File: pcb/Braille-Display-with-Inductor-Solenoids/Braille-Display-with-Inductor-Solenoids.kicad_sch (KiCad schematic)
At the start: 15 parts, among them J1 Screw_Terminal_01x02, J2 Screw_Terminal_01x02, J3 Screw_Terminal_01x02, SW1 SW_Push, SW2 SW_Push, U1 RP2040-Zero

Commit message: Remove symbol and footprint libraries
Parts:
- removed U1: RP2040-Zero, 00-project-footprint-lib:RP2040 Zero, symbol 00-project-symbol-lib:RP2040-Zero
- added U1: RP2040-Zero, 00-project-footprints:RP2040 Zero, symbol 00-project-symbols:RP2040-Zero
- SW1, SW2: footprint 00-project-footprint-lib:PushButtonSMD_2.93x3.9 -> 00-project-footprints:PushButtonSMD_2.93x3.9
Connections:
- net +3V3: now also U1.3 (3V3)
- net +5V: now also U1.1 (5V)
- net GND: now also U1.2 (GND)
- net SHIFT_G: now also U1.15 (GP5)
- net SHIFT_RCLK: now also U1.14 (GP4)
- net SHIFT_SER_IN: now also U1.12 (GP2)
- net SHIFT_SRCK: now also U1.13 (GP3)
- net SW_1: now also U1.5 (GP28)
- net SW_2: now also U1.6 (GP27)
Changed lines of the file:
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@@
 			)
 		)
-		(property "Footprint" "00-project-footprint-lib:PushButtonSMD_2.93x3.9"
+		(property "Footprint" "00-project-footprints:PushButtonSMD_2.93x3.9"
 			(at 67.31 158.75 0)
 			(effects
@@
 				(path "/3829a125-89bd-48f9-bfbe-92d753eb8f7f"
 					(reference "SW1")
-					(unit 1)
-				)
-			)
-		)
-	)
-	(symbol
-		(lib_id "00-project-symbol-lib:RP2040-Zero")
-		(at 64.77 48.26 0)
-		(unit 1)
-		(exclude_from_sim no)
-		(in_bom yes)
-		(on_board yes)
-		(dnp no)
-		(fields_autoplaced yes)
-		(property "Reference" "U1"
-			(at 64.77 35.56 0)
-			(effects
-				(font
-					(size 1.27 1.27)
-				)
-			)
-		)
-		(property "Value" "RP2040-Zero"
-			(at 64.77 38.1 0)
-			(effects
-				(font
-					(size 1.27 1.27)
-				)
-			)
-		)
-		(property "Footprint" "00-project-footprint-lib:RP2040 Zero"
-			(at 59.69 48.26 0)
-			(effects
-				(font
-					(size 1.27 1.27)
-				)
-				(hide yes)
-			)
-		)
-		(property "Datasheet" ""
-			(at 59.69 48.26 0)
-			(effects
-				(font
-					(size 1.27 1.27)
-				)
-				(hide yes)
-			)
-		)
-		(property "Description" ""
-			(at 64.77 48.26 0)
-			(effects
-				(font
-					(size 1.27 1.27)
-				)
-				(hide yes)
-			)
-		)
-		(pin "2"
-		)
-		(pin "21"
-		)
-		(pin "9"
-		)
-		(pin "17"
-		)
-		(pin "8"
-		)
-		(pin "19"
-		)
-		(pin "5"
-		)
-		(pin "18"
-		)
-		(pin "6"
-		)
-		(pin "20"
-		)
-		(pin "7"
-		)
-		(pin "4"
-		)
-		(pin "3"
-		)
-		(pin "23"
-		)
-		(pin "11"
-		)
-		(pin "14"
-		)
-		(pin "15"
-		)
-		(pin "22"
-		)
-		(pin "13"
-		)
-		(pin "12"
-		)
-		(pin "1"
-		)
-		(pin "10"
-		)
-		(pin "16"
-		)
-		(instances
-			(project ""
-				(path "/3829a125-89bd-48f9-bfbe-92d753eb8f7f"
-					(reference "U1")
 					(unit 1)
 				)
@@
 	)
 	(symbol
+		(lib_id "00-project-symbols:RP2040-Zero")
+		(at 64.77 48.26 0)
+		(unit 1)
+		(exclude_from_sim no)
+		(in_bom yes)
+		(on_board yes)
+		(dnp no)
+		(fields_autoplaced yes)
+		(property "Reference" "U1"
+			(at 64.77 35.56 0)
+			(effects
+				(font
+					(size 1.27 1.27)
+				)
+			)
+		)
+		(property "Value" "RP2040-Zero"
+			(at 64.77 38.1 0)
+			(effects
+				(font
+					(size 1.27 1.27)
+				)
+			)
+		)
+		(property "Footprint" "00-project-footprints:RP2040 Zero"
+			(at 59.69 48.26 0)
+			(effects
+				(font
+					(size 1.27 1.27)
+				)
+				(hide yes)
+			)
+		)
+		(property "Datasheet" ""
+			(at 59.69 48.26 0)
+			(effects
+				(font
+					(size 1.27 1.27)
+				)
+				(hide yes)
+			)
+		)
+		(property "Description" ""
+			(at 64.77 48.26 0)
+			(effects
+				(font
+					(size 1.27 1.27)
+				)
+				(hide yes)
+			)
+		)
+		(pin "14"
+		)
+		(pin "13"
+		)
+		(pin "11"
+		)
+		(pin "12"
+		)
+		(pin "15"
+		)
+		(pin "10"
+		)
+		(pin "8"
+		)
+		(pin "20"
+		)
+		(pin "3"
+		)
+		(pin "21"
+		)
+		(pin "5"
+		)
+		(pin "7"
+		)
+		(pin "16"
+		)
+		(pin "23"
+		)
+		(pin "17"
+		)
+		(pin "19"
+		)
+		(pin "22"
+		)
+		(pin "18"
+		)
+		(pin "2"
+		)
+		(pin "6"
+		)
+		(pin "4"
+		)
+		(pin "9"
+		)
+		(pin "1"
+		)
+		(instances
+			(project ""
+				(path "/3829a125-89bd-48f9-bfbe-92d753eb8f7f"
+					(reference "U1")
+					(unit 1)
+				)
+			)
+		)
+	)
+	(symbol
 		(lib_id "power:+3V3")
 		(at 44.45 48.26 90)
@@
 			)
 		)
-		(property "Footprint" "00-project-footprint-lib:PushButtonSMD_2.93x3.9"
+		(property "Footprint" "00-project-footprints:PushButtonSMD_2.93x3.9"
 			(at 85.09 158.75 0)
 			(effects

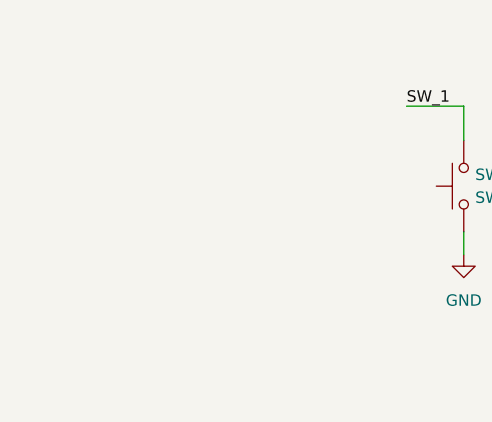
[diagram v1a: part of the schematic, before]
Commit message: Add both inductors on same PCB, switch to new drivers
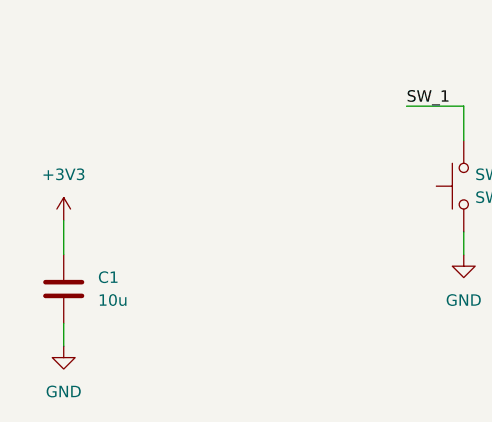
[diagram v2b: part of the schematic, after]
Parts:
- added C1: 10u, Capacitor_SMD:C_1206_3216Metric_Pad1.33x1.80mm_HandSolder, symbol Device:C
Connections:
- net +3V3: now also C1.1
- net GND: now also C1.2
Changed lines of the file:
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@@
+	(wire
+		(pts
+			(xy 27.94 162.56) (xy 27.94 166.37)
+		)
+		(stroke
+			(width 0)
+			(type default)
+		)
+	)
 	(wire
 		(pts
@@
 		(pts
 			(xy 90.17 149.86) (xy 90.17 153.67)
+		)
+		(stroke
+			(width 0)
+			(type default)
+		)
+	)
+	(wire
+		(pts
+			(xy 27.94 173.99) (xy 27.94 176.53)
 		)
 		(stroke
@@
 	)
 	(symbol
+		(lib_id "Device:C")
+		(at 27.94 170.18 0)
+		(unit 1)
+		(exclude_from_sim no)
+		(in_bom yes)
+		(on_board yes)
+		(dnp no)
+		(fields_autoplaced yes)
+		(property "Reference" "C1"
+			(at 31.75 168.9099 0)
+			(effects
+				(font
+					(size 1.27 1.27)
+				)
+				(justify left)
+			)
+		)
+		(property "Value" "10u"
+			(at 31.75 171.4499 0)
+			(effects
+				(font
+					(size 1.27 1.27)
+				)
+				(justify left)
+			)
+		)
+		(property "Footprint" "Capacitor_SMD:C_1206_3216Metric_Pad1.33x1.80mm_HandSolder"
+			(at 28.9052 173.99 0)
+			(effects
+				(font
+					(size 1.27 1.27)
+				)
+				(hide yes)
+			)
+		)
+		(property "Datasheet" "~"
+			(at 27.94 170.18 0)
+			(effects
+				(font
+					(size 1.27 1.27)
+				)
+				(hide yes)
+			)
+		)
+		(property "Description" "Unpolarized capacitor"
+			(at 27.94 170.18 0)
+			(effects
+				(font
+					(size 1.27 1.27)
+				)
+				(hide yes)
+			)
+		)
+		(pin "2"
+		)
+		(pin "1"
+		)
+		(instances
+			(project ""
+				(path "/3829a125-89bd-48f9-bfbe-92d753eb8f7f"
+					(reference "C1")
+					(unit 1)
+				)
+			)
+		)
+	)
+	(symbol
 		(lib_id "00-project-symbols:RP2040-Zero")
 		(at 64.77 48.26 0)
@@
 	)
 	(symbol
+		(lib_id "power:+3V3")
+		(at 27.94 162.56 0)
+		(unit 1)
+		(exclude_from_sim no)
+		(in_bom yes)
+		(on_board yes)
+		(dnp no)
+		(fields_autoplaced yes)
+		(property "Reference" "#PWR012"
+			(at 27.94 166.37 0)
+			(effects
+				(font
+					(size 1.27 1.27)
+				)
+				(hide yes)
+			)
+		)
+		(property "Value" "+3V3"
+			(at 27.94 157.48 0)
+			(effects
+				(font
+					(size 1.27 1.27)
+				)
+			)
+		)
+		(property "Footprint" ""
+			(at 27.94 162.56 0)
+			(effects
+				(font
+					(size 1.27 1.27)
+				)
+				(hide yes)
+			)
+		)
+		(property "Datasheet" ""
+			(at 27.94 162.56 0)
+			(effects
+				(font
+					(size 1.27 1.27)
+				)
+				(hide yes)
+			)
+		)
+		(property "Description" "Power symbol creates a global label with name \"+3V3\""
+			(at 27.94 162.56 0)
+			(effects
+				(font
+					(size 1.27 1.27)
+				)
+				(hide yes)
+			)
+		)
+		(pin "1"
+		)
+		(instances
+			(project "Braille-Display-with-Inductor-Solenoids"
+				(path "/3829a125-89bd-48f9-bfbe-92d753eb8f7f"
+					(reference "#PWR012")
+					(unit 1)
+				)
+			)
+		)
+	)
+	(symbol
 		(lib_id "Switch:SW_Push")
 		(at 90.17 158.75 90)
@@
 					(unit 1)
 				)
+			)
+		)
+	)
+	(symbol
+		(lib_id "power:GND")
+		(at 27.94 176.53 0)
+		(unit 1)
+		(exclude_from_sim no)
+		(in_bom yes)
+		(on_board yes)
+		(dnp no)
+		(fields_autoplaced yes)
+		(property "Reference" "#PWR011"
+			(at 27.94 182.88 0)
+			(effects
+				(font
+					(size 1.27 1.27)
+				)
+				(hide yes)
+			)
+		)
+		(property "Value" "GND"
+			(at 27.94 181.61 0)
+			(effects
+				(font
+					(size 1.27 1.27)
+				)
+			)
+		)
+		(property "Footprint" ""
+			(at 27.94 176.53 0)
+			(effects
+				(font
+					(size 1.27 1.27)
+				)
+				(hide yes)
+			)
+		)
+		(property "Datasheet" ""
+			(at 27.94 176.53 0)
+			(effects
+				(font
+					(size 1.27 1.27)
+				)
+				(hide yes)
+			)
+		)
+		(property "Description" "Power symbol creates a global label with name \"GND\" , ground"
+			(at 27.94 176.53 0)
+			(effects
+				(font
+					(size 1.27 1.27)
+				)
+				(hide yes)
+			)
+		)
+		(pin "1"
+		)
+		(instances
+			(project ""
+				(path "/3829a125-89bd-48f9-bfbe-92d753eb8f7f"
+					(reference "#PWR011")
+					(unit 1)
+				)

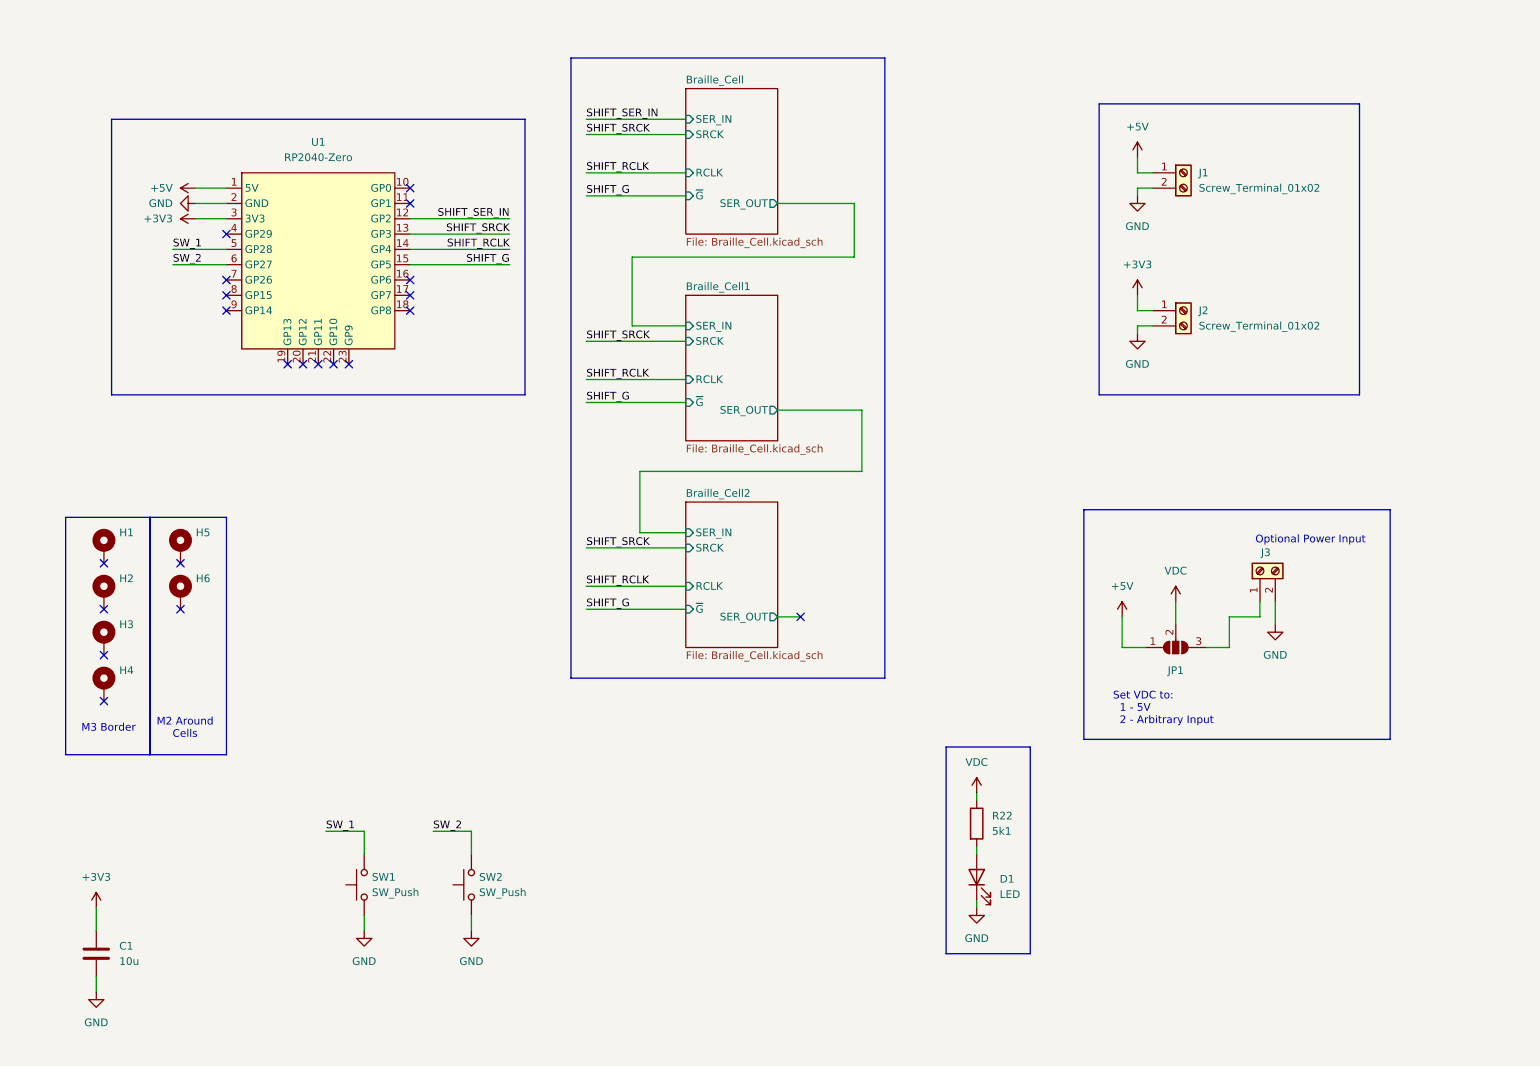
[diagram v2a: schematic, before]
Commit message: Add breakouts, shrink SMD vertical inductor cutouts, add braille cell (4x now)
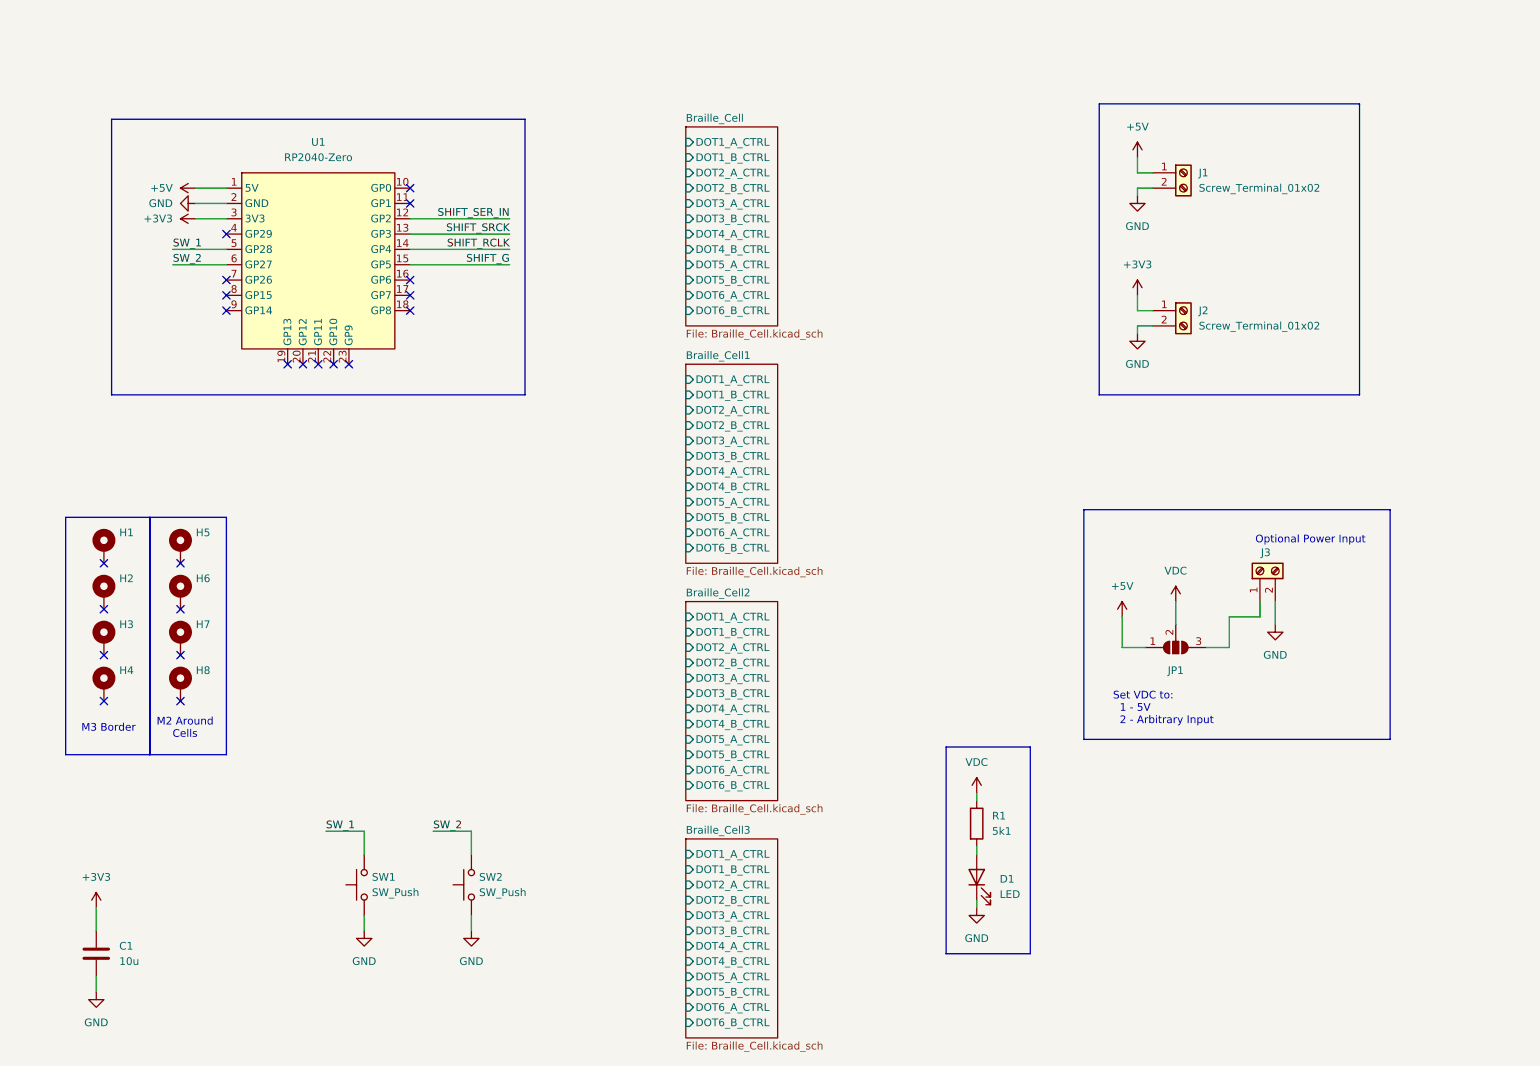
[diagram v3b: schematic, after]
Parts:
- added H7, H8: MountingHole_Pad, 00-project-footprints:Braille_Block_MountingHoles_M2_3x, symbol Mechanical:MountingHole_Pad
- H5, H6: footprint MountingHole:MountingHole_2.2mm_M2_Pad -> 00-project-footprints:Braille_Block_MountingHoles_M2_3x
- renumbered R22 to R1
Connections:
- no-connect marks 21 -> 22
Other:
- added sheet Braille_Cell3 (Braille_Cell.kicad_sch)
- sheet Braille_Cell ports: added DOT1_A_CTRL, DOT1_B_CTRL, DOT2_A_CTRL, DOT2_B_CTRL, DOT3_A_CTRL, DOT3_B_CTRL, DOT4_A_CTRL, DOT4_B_CTRL, DOT5_A_CTRL, DOT5_B_CTRL, DOT6_A_CTRL, DOT6_B_CTRL; removed RCLK, SER_IN, SER_OUT, SRCK, ~{G}
- sheet Braille_Cell1 ports: added DOT1_A_CTRL, DOT1_B_CTRL, DOT2_A_CTRL, DOT2_B_CTRL, DOT3_A_CTRL, DOT3_B_CTRL, DOT4_A_CTRL, DOT4_B_CTRL, DOT5_A_CTRL, DOT5_B_CTRL, DOT6_A_CTRL, DOT6_B_CTRL; removed RCLK, SER_IN, SER_OUT, SRCK, ~{G}
- sheet Braille_Cell2 ports: added DOT1_A_CTRL, DOT1_B_CTRL, DOT2_A_CTRL, DOT2_B_CTRL, DOT3_A_CTRL, DOT3_B_CTRL, DOT4_A_CTRL, DOT4_B_CTRL, DOT5_A_CTRL, DOT5_B_CTRL, DOT6_A_CTRL, DOT6_B_CTRL; removed RCLK, SER_IN, SER_OUT, SRCK, ~{G}

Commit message: Change page layout and reconnect components
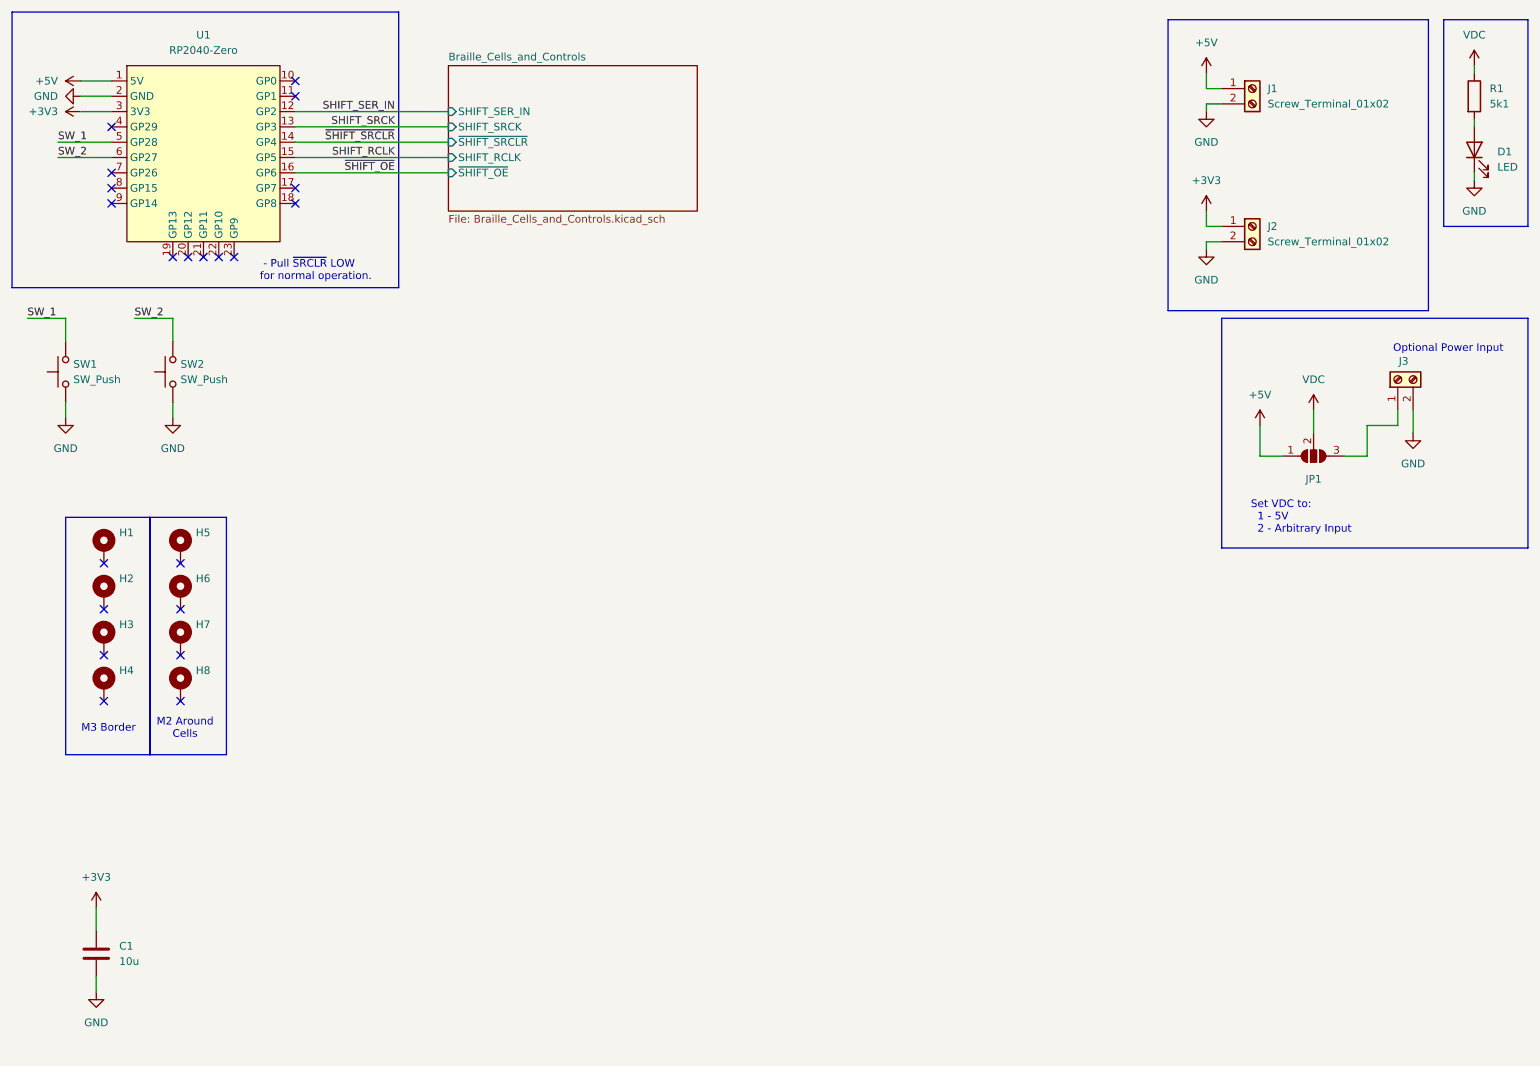
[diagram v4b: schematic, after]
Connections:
- net SHIFT_G is gone; now on net SHIFT_RCLK: U1.15 (GP5)
- net SHIFT_RCLK: no longer U1.14 (GP4)
- net ~{SHIFT_OE}: now reaches U1.16 (GP6)
- new net ~{SHIFT_SRCLR}: U1.14 (GP4)
- no-connect marks 22 -> 21
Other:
- removed sheet Braille_Cell
- removed sheet Braille_Cell1
- removed sheet Braille_Cell2
- removed sheet Braille_Cell3
- added sheet Braille_Cells_and_Controls (Braille_Cells_and_Controls.kicad_sch)
- note added: "- Pull ~{SRCLR} LOW for normal operation."
- moved on the sheet: D1, J1, J2, J3, JP1, R1, SW1, SW2, U1
